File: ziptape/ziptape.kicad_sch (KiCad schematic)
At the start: 11 parts

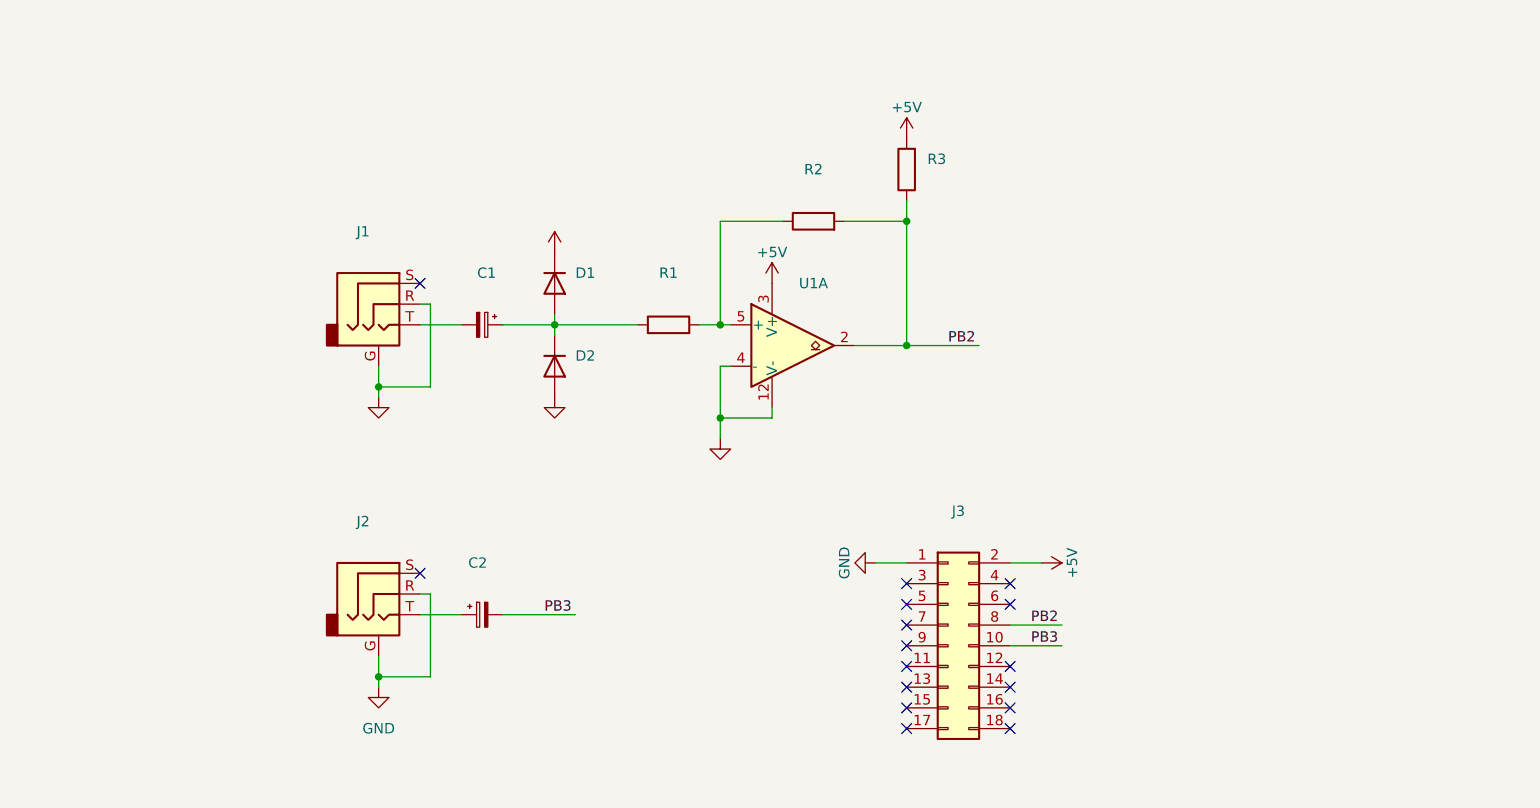
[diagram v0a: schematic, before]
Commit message: Assign footprints
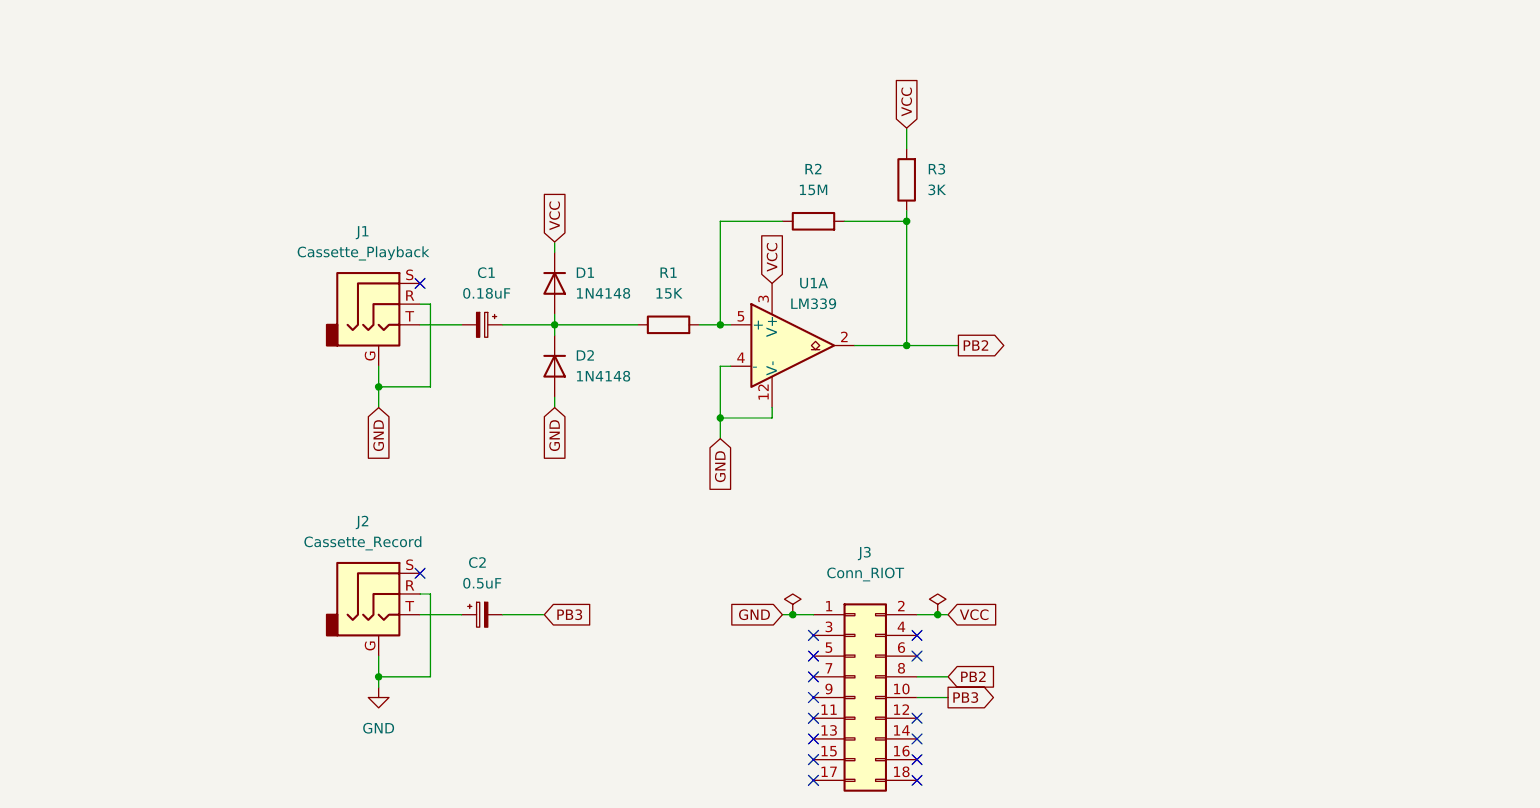
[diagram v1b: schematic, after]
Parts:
- C1: value (none) -> 0.18uF; footprint (none) -> Capacitor_THT:CP_Radial_D5.0mm_P2.50mm
- C2: value (none) -> 0.5uF; footprint (none) -> Capacitor_THT:CP_Radial_D5.0mm_P2.50mm
- D1, D2: value (none) -> 1N4148; footprint (none) -> Diode_THT:D_DO-35_SOD27_P7.62mm_Horizontal
- J1: value (none) -> Cassette_Playback; footprint (none) -> Connector_Jack:Jack_3.5mm_4Pole_TRRS
- J2: value (none) -> Cassette_Record; footprint (none) -> Connector_Jack:Jack_3.5mm_4Pole_TRRS
- J3: value (none) -> Conn_RIOT; footprint (none) -> Connector_PinHeader_2.54mm:PinHeader_2x09_P2.54mm_Vertical
- R1: value (none) -> 15K; footprint (none) -> Resistor_THT:R_Axial_DIN0207_L6.3mm_D2.5mm_P7.62mm_Horizontal
- R2: value (none) -> 15M; footprint (none) -> Resistor_THT:R_Axial_DIN0207_L6.3mm_D2.5mm_P7.62mm_Horizontal
- R3: value (none) -> 3K; footprint (none) -> Resistor_THT:R_Axial_DIN0207_L6.3mm_D2.5mm_P7.62mm_Horizontal
- U1: value (none) -> LM339; footprint (none) -> Package_DIP:DIP-14_W7.62mm
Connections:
- net +5V renamed VCC
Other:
- company: (none) -> Plastic Objects
- title: (none) -> Zip Tape Adapter
- moved on the sheet: J3, R3

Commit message: Add layout
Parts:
- added J4: Conn_Adapter_A, Connector_PinSocket_2.54mm:PinSocket_2x09_P2.54mm_Vertical, symbol Connector_Generic:Conn_02x09_Odd_Even
- added J5: (no value), symbol Connector_Generic:Conn_02x09_Odd_Even
- J3: value Conn_RIOT -> (none); footprint Connector_PinHeader_2.54mm:PinHeader_2x09_P2.54mm_Vertical -> (none)
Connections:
- new net A_GND: J4.1 (Pin_1)
- new net A_PA0: J4.3 (Pin_3)
- new net A_PA1: J4.5 (Pin_5)
- new net A_PA2: J4.7 (Pin_7)
- new net A_PA3: J4.9 (Pin_9)
- new net A_PA4: J4.11 (Pin_11)
- new net A_PA5: J4.13 (Pin_13)
- new net A_PA6: J4.15 (Pin_15)
- new net A_PA7: J4.17 (Pin_17)
- new net A_PB0: J4.4 (Pin_4)
- new net A_PB1: J4.6 (Pin_6)
- new net A_PB2: J4.8 (Pin_8)
- new net A_PB3: J4.10 (Pin_10)
- new net A_PB4: J4.12 (Pin_12)
- new net A_PB5: J4.14 (Pin_14)
- new net A_PB6: J4.16 (Pin_16)
- new net A_PB7: J4.18 (Pin_18)
- new net A_VCC: J4.2 (Pin_2)
- new net B_GND: J5.1 (Pin_1)
- new net B_PA0: J5.3 (Pin_3)
- new net B_PA1: J5.5 (Pin_5)
- new net B_PA2: J5.7 (Pin_7)
- new net B_PA3: J5.9 (Pin_9)
- new net B_PA4: J5.11 (Pin_11)
- new net B_PA5: J5.13 (Pin_13)
- new net B_PA6: J5.15 (Pin_15)
- new net B_PA7: J5.17 (Pin_17)
- new net B_PB0: J5.4 (Pin_4)
- new net B_PB1: J5.6 (Pin_6)
- new net B_PB2: J5.8 (Pin_8)
- new net B_PB3: J5.10 (Pin_10)
- new net B_PB4: J5.12 (Pin_12)
- new net B_PB5: J5.14 (Pin_14)
- new net B_PB6: J5.16 (Pin_16)
- new net B_PB7: J5.18 (Pin_18)
- new net B_VCC: J5.2 (Pin_2)
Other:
- note added: "RIOT Adapter"
- moved on the sheet: C1, C2, D1, D2, J1, J2, J3, R1, R2, R3, U1A

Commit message: Update schema
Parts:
- J3: value (none) -> Conn_RIOT; footprint (none) -> Connector_PinHeader_2.54mm:PinHeader_2x09_P2.54mm_Vertical
- J5: value (none) -> Conn_Adapter_B; footprint (none) -> Connector_PinSocket_2.54mm:PinSocket_2x09_P2.54mm_Vertical
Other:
- company: Plastic Objects -> Plastic Objects Limited
- title: Zip Tape Adapter -> PAL-1 Zip Tape Adapter
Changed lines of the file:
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@@
   (paper "A4")
   (title_block
-    (title "Zip Tape Adapter")
+    (title "PAL-1 Zip Tape Adapter")
     (date "Jan 2023")
     (rev "1.0a")
-    (company "Plastic Objects")
+    (company "Plastic Objects Limited")
   )
   (junction (at 203.2 67.31) (diameter 0) (color 0 0 0 0)
@@
     (in_bom yes) (on_board yes)
     (property "Reference" "J5" (id 0) (at 81.28 46.99 0))
-    (property "Value" "" (id 1) (at 81.28 49.53 0))
-    (property "Footprint" "" (id 2) (at 80.01 64.77 0)
+    (property "Value" "Conn_Adapter_B" (id 1) (at 81.28 49.53 0))
+    (property "Footprint" "Connector_PinSocket_2.54mm:PinSocket_2x09_P2.54mm_Vertical" (id 2) (at 80.01 64.77 0)
       (effects (font (size 1.27 1.27)) hide)
     )
@@
     (in_bom yes) (on_board yes)
     (property "Reference" "J3" (id 0) (at 198.12 92.71 0))
-    (property "Value" "" (id 1) (at 198.12 95.25 0))
-    (property "Footprint" "" (id 2) (at 196.85 110.49 0)
-      (effects (font (size 1.27 1.27)) hide)
-    )
+    (property "Value" "Conn_RIOT" (id 1) (at 198.12 95.25 0))
+    (property "Footprint" "Connector_PinHeader_2.54mm:PinHeader_2x09_P2.54mm_Vertical" (id 2) (at 196.85 110.49 0)
+      (effects (font (size 1.27 1.27)) hide)
+    )
